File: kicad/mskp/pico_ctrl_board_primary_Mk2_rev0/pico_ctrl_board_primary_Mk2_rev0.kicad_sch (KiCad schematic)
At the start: 23 parts, among them J1 USB_C_I2C_Receptacle, J2 SPI-JST, J3 RJ45_I2C_SPI_Port, J4 UART-JST, J5 I2C-aux-pad, J6 OLED_128x64, J7 Keypad-Matrix, J8 USB-sw-ctrl, SW1 RESET, U1 Raspberry_Pi_Pico

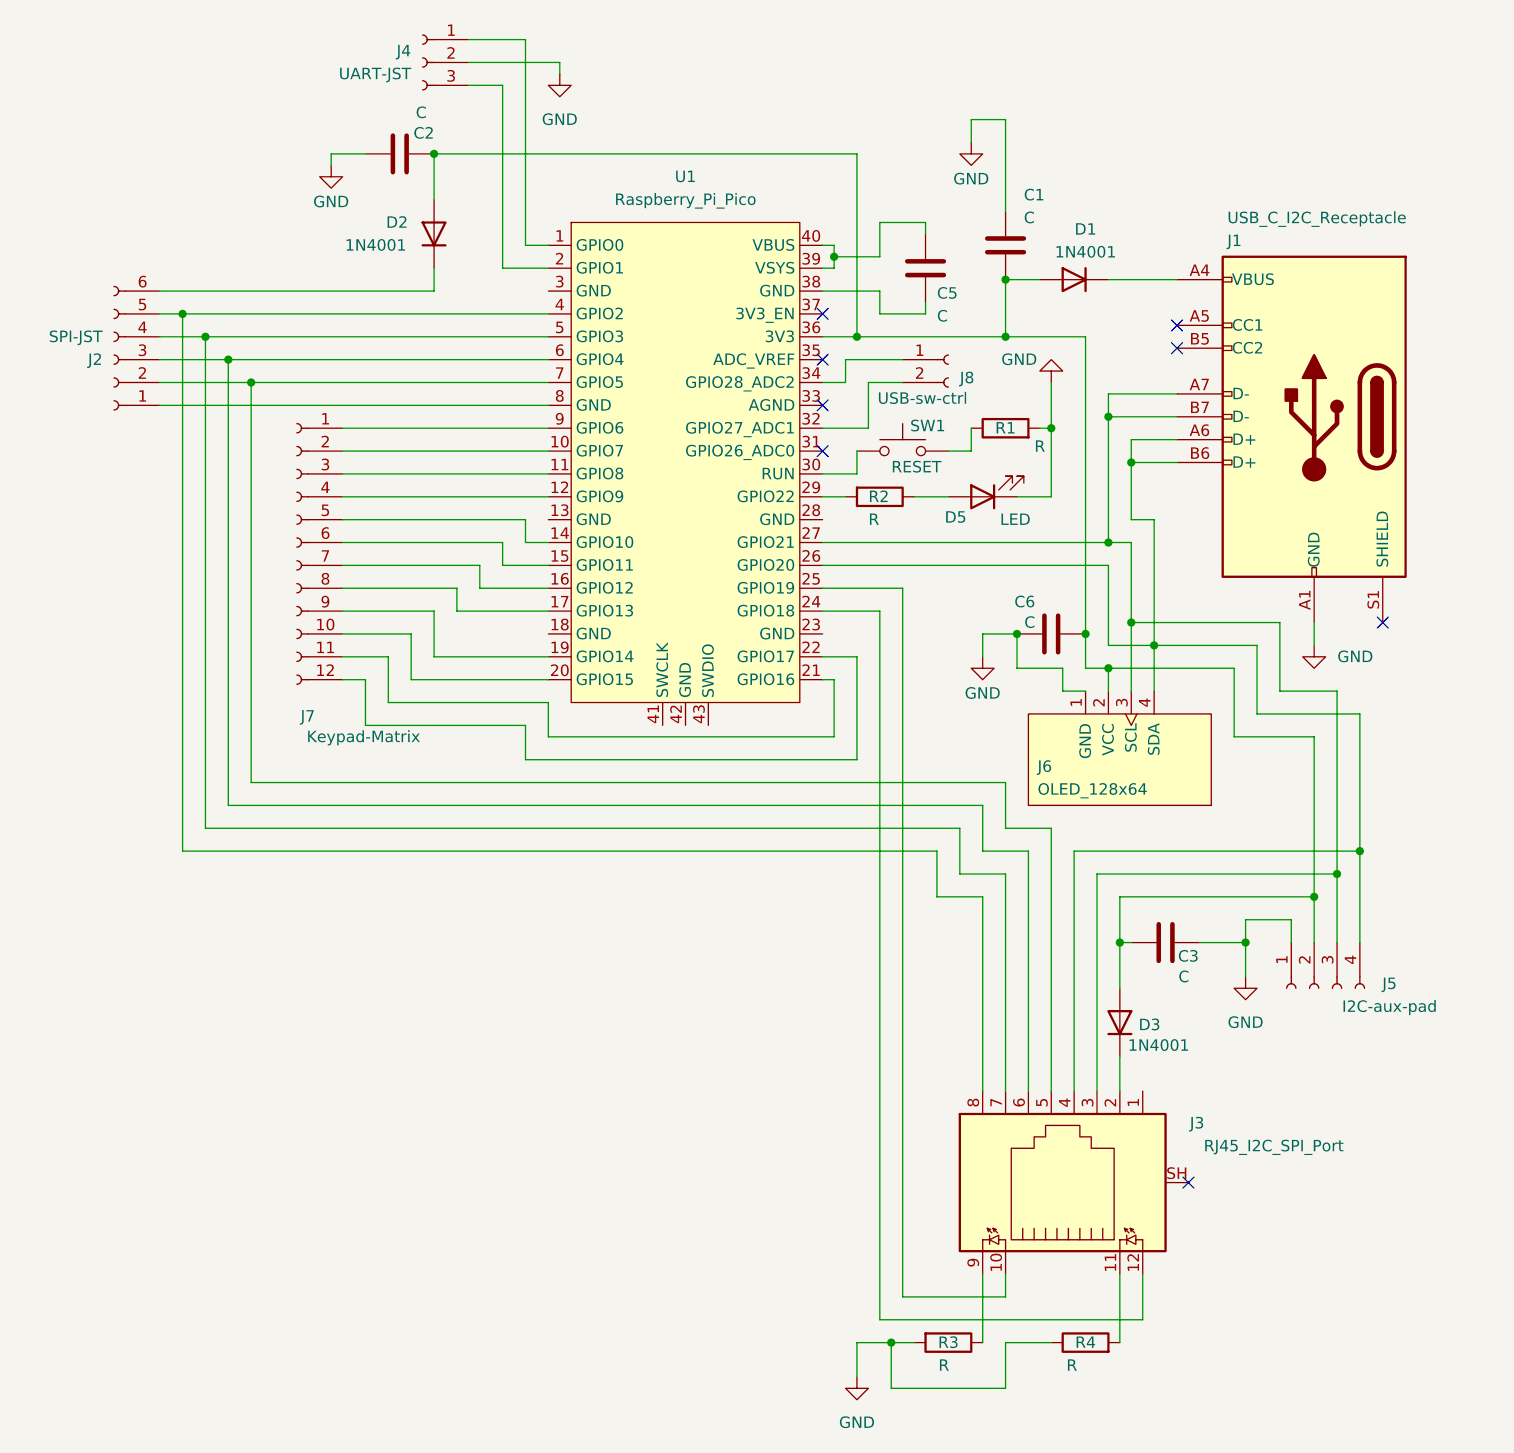
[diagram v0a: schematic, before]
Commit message: Adds first drafts of adc mouse and io expander mk2
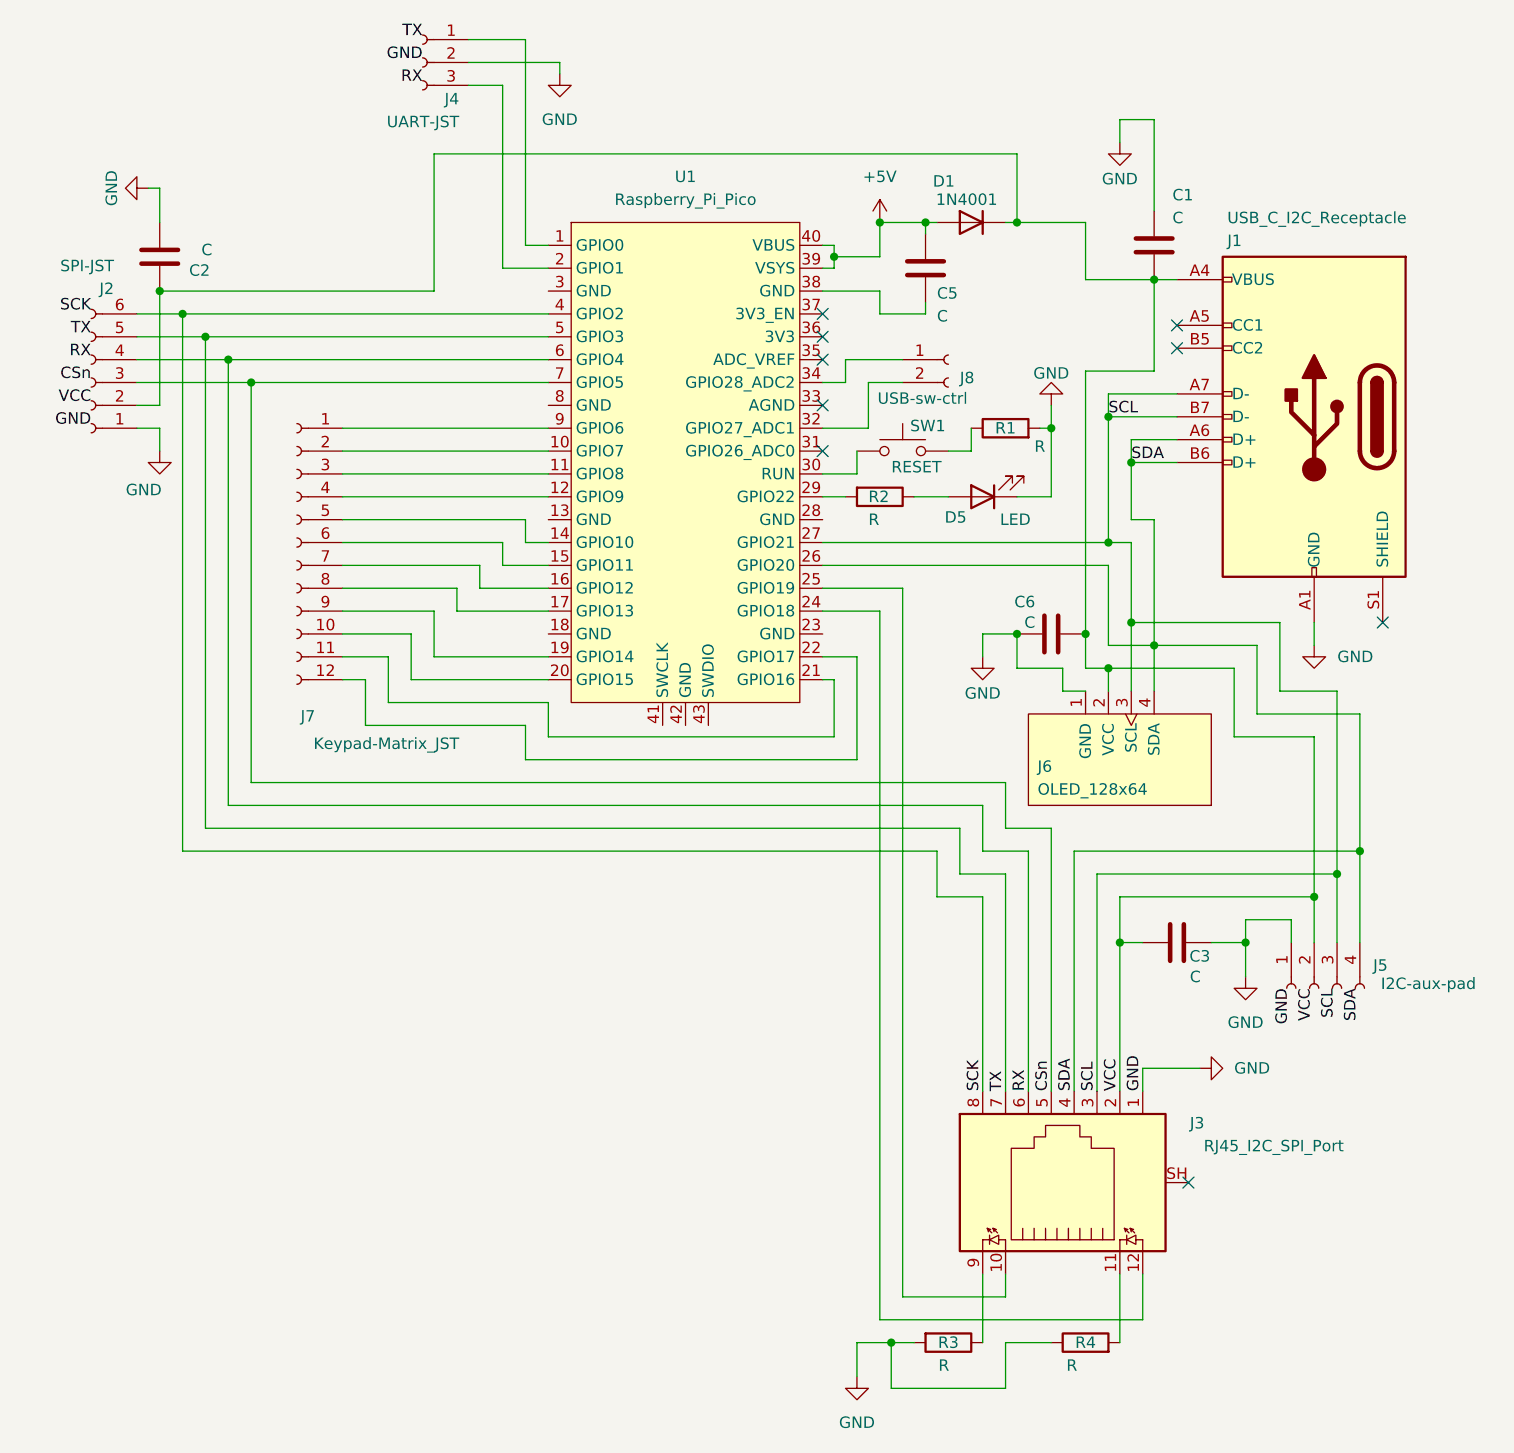
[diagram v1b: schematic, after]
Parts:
- removed D2, D3: 1N4001, Diode_THT:D_DO-41_SOD81_P10.16mm_Horizontal, symbol Diode:1N4001
- J7: value Keypad-Matrix -> Keypad-Matrix_JST
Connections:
- net GND: now also J2.1 (Pin_1), J3.1
- net VCC: now reaches J3.2
- net VCC: now also C1.1, C2.1, C3.2, C6.1, D1.1 (K), J1.A4 (VBUS), J1.A9 (VBUS), J1.B4 (VBUS), J1.B9 (VBUS), J2.2 (Pin_2), J5.2 (Pin_2), J6.2 (VCC)
- net SCK: now reaches J2.6 (Pin_6)
- net SCK: now also J3.8, U1.4 (GPIO2)
- net SDA: now reaches J1.A6 (D+), J1.B6 (D+), J3.4, J5.4 (Pin_4), J6.4 (SDA), U1.26 (GPIO20)
- net SCL: now reaches J1.A7 (D-), J1.B7 (D-), J3.3, J5.3 (Pin_3), J6.3 (SCL), U1.27 (GPIO21)
- net +5V: now reaches C5.1, U1.39 (VSYS), U1.40 (VBUS)
- net +5V: now also D1.2 (A)
- net TX: now reaches J3.7, U1.5 (GPIO3)
- net TX: now also J2.5 (Pin_5); no longer J2.4 (Pin_4)
- net RX: now reaches J3.6, U1.6 (GPIO4)
- net RX: now also J2.4 (Pin_4); no longer J2.3 (Pin_3)
- net CSn: now reaches J3.5, U1.7 (GPIO5)
- net CSn: now also J2.3 (Pin_3); no longer J2.2 (Pin_2)
- net at U1.8 (GND): no longer J2.1 (Pin_1)
- now unconnected: U1.36 (3V3)
- no-connect marks 8 -> 9
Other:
- moved on the sheet: C1, C2, C3, D1, J2

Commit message: Further refinement of first drafts adding specific components
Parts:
- added J9: Debug_pads, symbol Connector:Conn_01x03_Socket
- C1, C3: value C -> 22uF
- C5: value C -> 100uF
- C6: value C -> 100nF
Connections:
- net GND: now also C5.2, U1.38 (GND), U1.42 (GND), J9.2 (Pin_2)
- net SEL: now reaches J8.1 (Pin_1), U1.34 (GPIO28_ADC2)
- net SUS: now reaches J8.2 (Pin_2), U1.32 (GPIO27_ADC1)
- net SWCLK: now reaches U1.41 (SWCLK)
- net SWCLK: now also J9.3 (Pin_3)
- net SWDIO: now reaches U1.43 (SWDIO)
- net SWDIO: now also J9.1 (Pin_1)
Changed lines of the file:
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@@
 		(color 0 0 0 0)
 	)
+	(junction
+		(at 144.78 53.34)
+		(diameter 0)
+		(color 0 0 0 0)
+	)
 	(no_connect
 		(at 133.35 63.5)
@@
 	(wire
 		(pts
-			(xy 139.7 50.8) (xy 133.35 50.8)
+			(xy 118.11 99.06) (xy 118.11 120.65)
 		)
 		(stroke
@@
 	(wire
 		(pts
+			(xy 133.35 50.8) (xy 140.97 50.8)
+		)
+		(stroke
+			(width 0)
+			(type default)
+		)
+	)
+	(wire
+		(pts
 			(xy 165.1 92.71) (xy 165.1 95.25)
 		)
@@
 	(wire
 		(pts
-			(xy 144.78 53.34) (xy 139.7 53.34)
+			(xy 144.78 53.34) (xy 140.97 53.34)
 		)
 		(stroke
@@
 	(wire
 		(pts
+			(xy 115.57 99.06) (xy 115.57 120.65)
+		)
+		(stroke
+			(width 0)
+			(type default)
+		)
+	)
+	(wire
+		(pts
 			(xy 151.13 107.95) (xy 151.13 113.03)
 		)
@@
 	(wire
 		(pts
-			(xy 144.78 52.07) (xy 144.78 53.34)
-		)
-		(stroke
-			(width 0)
-			(type default)
-		)
-	)
-	(wire
-		(pts
 			(xy 102.87 48.26) (xy 97.79 48.26)
 		)
@@
 	(wire
 		(pts
+			(xy 144.78 53.34) (xy 144.78 52.07)
+		)
+		(stroke
+			(width 0)
+			(type default)
+		)
+	)
+	(wire
+		(pts
+			(xy 144.78 53.34) (xy 151.13 53.34)
+		)
+		(stroke
+			(width 0)
+			(type default)
+		)
+	)
+	(wire
+		(pts
 			(xy 166.37 160.02) (xy 166.37 167.64)
 		)
@@
 	(wire
 		(pts
-			(xy 139.7 53.34) (xy 139.7 50.8)
+			(xy 140.97 53.34) (xy 140.97 50.8)
 		)
 		(stroke
@@
 	(wire
 		(pts
+			(xy 120.65 99.06) (xy 120.65 120.65)
+		)
+		(stroke
+			(width 0)
+			(type default)
+		)
+	)
+	(wire
+		(pts
 			(xy 167.64 67.31) (xy 172.72 67.31)
 		)
@@
 		)
 	)
+	(label "GND"
+		(at 118.11 120.65 90)
+		(fields_autoplaced yes)
+		(effects
+			(font
+				(size 1.27 1.27)
+			)
+			(justify left bottom)
+		)
+	)
 	(label "CSn"
 		(at 158.75 139.7 90)
@@
 		)
 	)
+	(label "SEL"
+		(at 135.89 58.42 0)
+		(fields_autoplaced yes)
+		(effects
+			(font
+				(size 1.27 1.27)
+			)
+			(justify left bottom)
+		)
+	)
 	(label "SDA"
 		(at 193.04 128.27 270)
@@
 		)
 	)
+	(label "SWCLK"
+		(at 115.57 120.65 90)
+		(fields_autoplaced yes)
+		(effects
+			(font
+				(size 1.27 1.27)
+			)
+			(justify left bottom)
+		)
+	)
 	(label "SDA"
 		(at 167.64 69.85 0)
@@
 		)
 	)
+	(label "SWDIO"
+		(at 120.65 120.65 90)
+		(fields_autoplaced yes)
+		(effects
+			(font
+				(size 1.27 1.27)
+			)
+			(justify left bottom)
+		)
+	)
 	(label "SCL"
 		(at 190.5 128.27 270)
@@
 		)
 	)
+	(label "SUS"
+		(at 138.43 60.96 0)
+		(fields_autoplaced yes)
+		(effects
+			(font
+				(size 1.27 1.27)
+			)
+			(justify left bottom)
+		)
+	)
 	(label "GND"
 		(at 52.07 66.04 180)
@@
 			)
 		)
-		(property "Value" "C"
+		(property "Value" "22uF"
 			(at 172.212 42.672 0)
 			(effects
@@
 	)
 	(symbol
+		(lib_id "power:GND")
+		(at 151.13 53.34 0)
+		(unit 1)
+		(exclude_from_sim no)
+		(in_bom yes)
+		(on_board yes)
+		(dnp no)
+		(property "Reference" "#PWR012"
+			(at 151.13 59.69 0)
+			(effects
+				(font
+					(size 1.27 1.27)
+				)
+				(hide yes)
+			)
+		)
+		(property "Value" "GND"
+			(at 151.13 56.896 0)
+			(effects
+				(font
+					(size 1.27 1.27)
+				)
+			)
+		)
+		(property "Footprint" ""
+			(at 151.13 53.34 0)
+			(effects
+				(font
+					(size 1.27 1.27)
+				)
+				(hide yes)
+			)
+		)
+		(property "Datasheet" ""
+			(at 151.13 53.34 0)
+			(effects
+				(font
+					(size 1.27 1.27)
+				)
+				(hide yes)
+			)
+		)
+		(property "Description" "Power symbol creates a global label with name \"GND\" , ground"
+			(at 151.13 53.34 0)
+			(effects
+				(font
+					(size 1.27 1.27)
+				)
+				(hide yes)
+			)
+		)
+		(pin "1"
+		)
+		(instances
+			(project "pico_ctrl_board_primary_Mk2_rev0"
+				(path "/21b8209d-c157-4e20-9e4d-49b2b440c38a"
+					(reference "#PWR012")
+					(unit 1)
+				)
+			)
+		)
+	)
+	(symbol
 		(lib_id "ScottoKeebs:MCU_Raspberry_Pi_Pico")
 		(at 118.11 69.85 0)
@@
 			)
 		)
-		(property "Value" "C"
+		(property "Value" "100nF"
 			(at 156.972 87.63 90)
 			(effects
@@
 			)
 		)
-		(property "Value" "C"
+		(property "Value" "22uF"
 			(at 174.752 127 90)
 			(effects
@@
 		(dnp no)
 		(property "Reference" "C5"
-			(at 146.05 51.054 0)
+			(at 147.32 46.482 0)
 			(effects
 				(font
@@
 			)
 		)
-		(property "Value" "C"
-			(at 146.05 53.594 0)
+		(property "Value" "100uF"
+			(at 147.32 49.022 0)
 			(effects
 				(font
@@
 					(unit 1)
 				)
+			)
+		)
+	)
+	(symbol
+		(lib_id "Connector:Conn_01x03_Socket")
+		(at 118.11 125.73 270)
+		(unit 1)
+		(exclude_from_sim no)
+		(in_bom yes)
+		(on_board yes)
+		(dnp no)
+		(property "Reference" "J9"
+			(at 111.76 125.73 90)
+			(effects
+				(font
+					(size 1.27 1.27)
+				)
+			)
+		)
+		(property "Value" "Debug_pads"
+			(at 116.332 128.016 90)
+			(effects
+				(font
+					(size 1.27 1.27)
+				)
+			)
+		)
+		(property "Footprint" ""
+			(at 118.11 125.73 0)
+			(effects
+				(font
+					(size 1.27 1.27)
+				)
+				(hide yes)
+			)
+		)
+		(property "Datasheet" "~"
+			(at 118.11 125.73 0)
+			(effects
+				(font
+					(size 1.27 1.27)
+				)
+				(hide yes)
+			)
+		)
+		(property "Description" "Generic connector, single row, 01x03, script generated"
+			(at 118.11 125.73 0)
+			(effects
+				(font
+					(size 1.27 1.27)
+				)
+				(hide yes)
+			)
+		)
+		(pin "1"
+		)
+		(pin "2"
+		)
+		(pin "3"
+		)
+		(instances
+			(project "pico_ctrl_board_primary_Mk2_rev0"
+				(path "/21b8209d-c157-4e20-9e4d-49b2b440c38a"
+					(reference "J9")
+					(unit 1)
+				)

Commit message: Initital footprint assignment to all control boards
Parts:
- removed D1: 1N4001, Diode_THT:D_DO-41_SOD81_P10.16mm_Horizontal, symbol Diode:1N4001
- added D1, D2, D3: 1N5817, Diode_THT:D_DO-41_SOD81_P10.16mm_Horizontal, symbol Diode:1N5817
- C1, C3, C5, C6: footprint (none) -> Capacitor_SMD:C_1206_3216Metric_Pad1.33x1.80mm_HandSolder
- C2: value C -> 22uF; footprint (none) -> Capacitor_SMD:C_1206_3216Metric_Pad1.33x1.80mm_HandSolder
- D5: footprint (none) -> LED_SMD:LED_0805_2012Metric_Pad1.15x1.40mm_HandSolder
- J1: footprint (none) -> Connector_USB:USB_C_Receptacle_GCT_USB4110
- J2: footprint (none) -> Connector_JST:JST_GH_SM06B-GHS-TB_1x06-1MP_P1.25mm_Horizontal
- J3: footprint (none) -> Connector_RJ:RJ45_Amphenol_RJHSE538X
- J4: footprint (none) -> Connector_JST:JST_SH_SM03B-SRSS-TB_1x03-1MP_P1.00mm_Horizontal
- J5: footprint (none) -> Connector_PinHeader_2.54mm:PinHeader_1x04_P2.54mm_Vertical
- J7: footprint (none) -> Connector_JST:JST_GH_SM12B-GHS-TB_1x12-1MP_P1.25mm_Horizontal
- J8: footprint (none) -> Connector_PinHeader_2.54mm:PinHeader_1x02_P2.54mm_Vertical
- J9: footprint (none) -> Connector_PinHeader_2.54mm:PinHeader_1x03_P2.54mm_Vertical
- R1: value R -> 10K; footprint (none) -> Resistor_THT:R_Axial_DIN0207_L6.3mm_D2.5mm_P7.62mm_Horizontal
- R2, R3, R4: footprint (none) -> Resistor_THT:R_Axial_DIN0207_L6.3mm_D2.5mm_P7.62mm_Horizontal
- SW1: footprint (none) -> Button_Switch_SMD:SW_SPST_Omron_B3FS-101xP
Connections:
- net +5V: now also C2.1, C3.2, C6.1, J2.2 (Pin_2), J6.2 (VCC), D1.2 (A), D2.2 (A), D3.2 (A)
- net VCC: now also D3.1 (K); no longer C1.1, C2.1, C3.2, C6.1, J1.A4 (VBUS), J1.A9 (VBUS), J1.B4 (VBUS), J1.B9 (VBUS), J2.2 (Pin_2), J5.2 (Pin_2), J6.2 (VCC)
- new net: C1.1, D1.1 (K), J1.A4 (VBUS), J1.A9 (VBUS), J1.B4 (VBUS), J1.B9 (VBUS)
- new net: D2.1 (K), J5.2 (Pin_2)
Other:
- moved on the sheet: C6

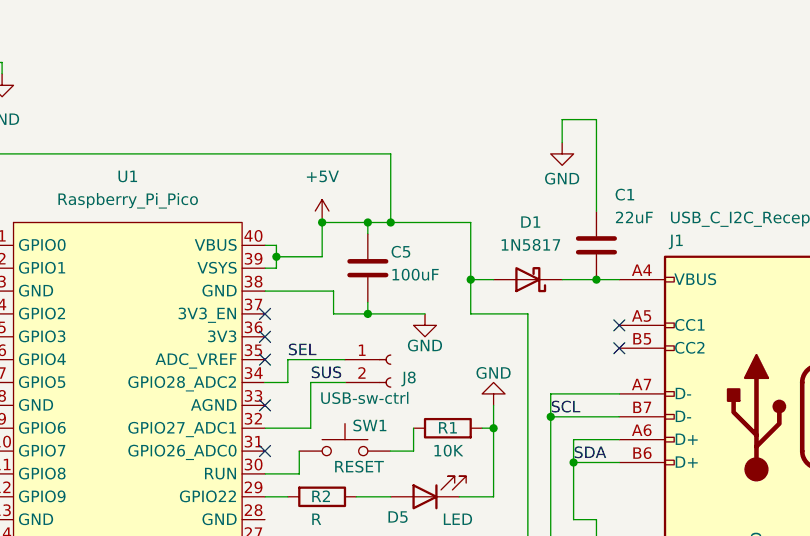
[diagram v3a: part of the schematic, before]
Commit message: Begins rough PCB part grouping for all control board revisions
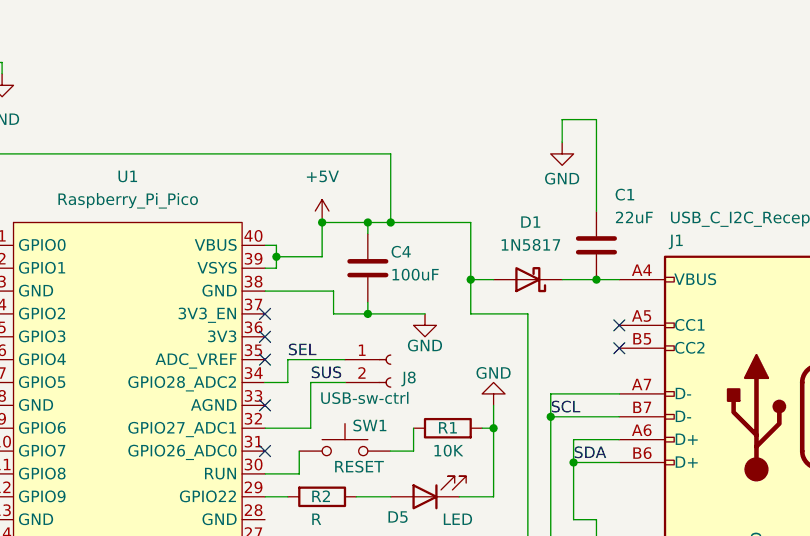
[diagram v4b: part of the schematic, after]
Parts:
- renumbered C5 to C4
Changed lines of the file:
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@@
 		(on_board yes)
 		(dnp no)
-		(property "Reference" "C5"
+		(property "Reference" "C4"
 			(at 147.32 46.482 0)
 			(effects
@@
 			(project "pico_ctrl_board_primary_Mk2_rev0"
 				(path "/21b8209d-c157-4e20-9e4d-49b2b440c38a"
-					(reference "C5")
+					(reference "C4")
 					(unit 1)
 				)
